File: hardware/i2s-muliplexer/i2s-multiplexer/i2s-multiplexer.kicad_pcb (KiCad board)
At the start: 2 copper layers, 80 x 50 mm, 35 parts, among them J1 Conn_01x05, J2 Conn_01x05, J3 Conn_01x05, J4 Conn_01x05, J5 Conn_01x05, J6 Conn_01x05, J7 Conn_01x07, J8 Conn_01x05, U1 74HC244, U2 74HC244, U3 74HC244, U4 74HC126, U5 74LS138

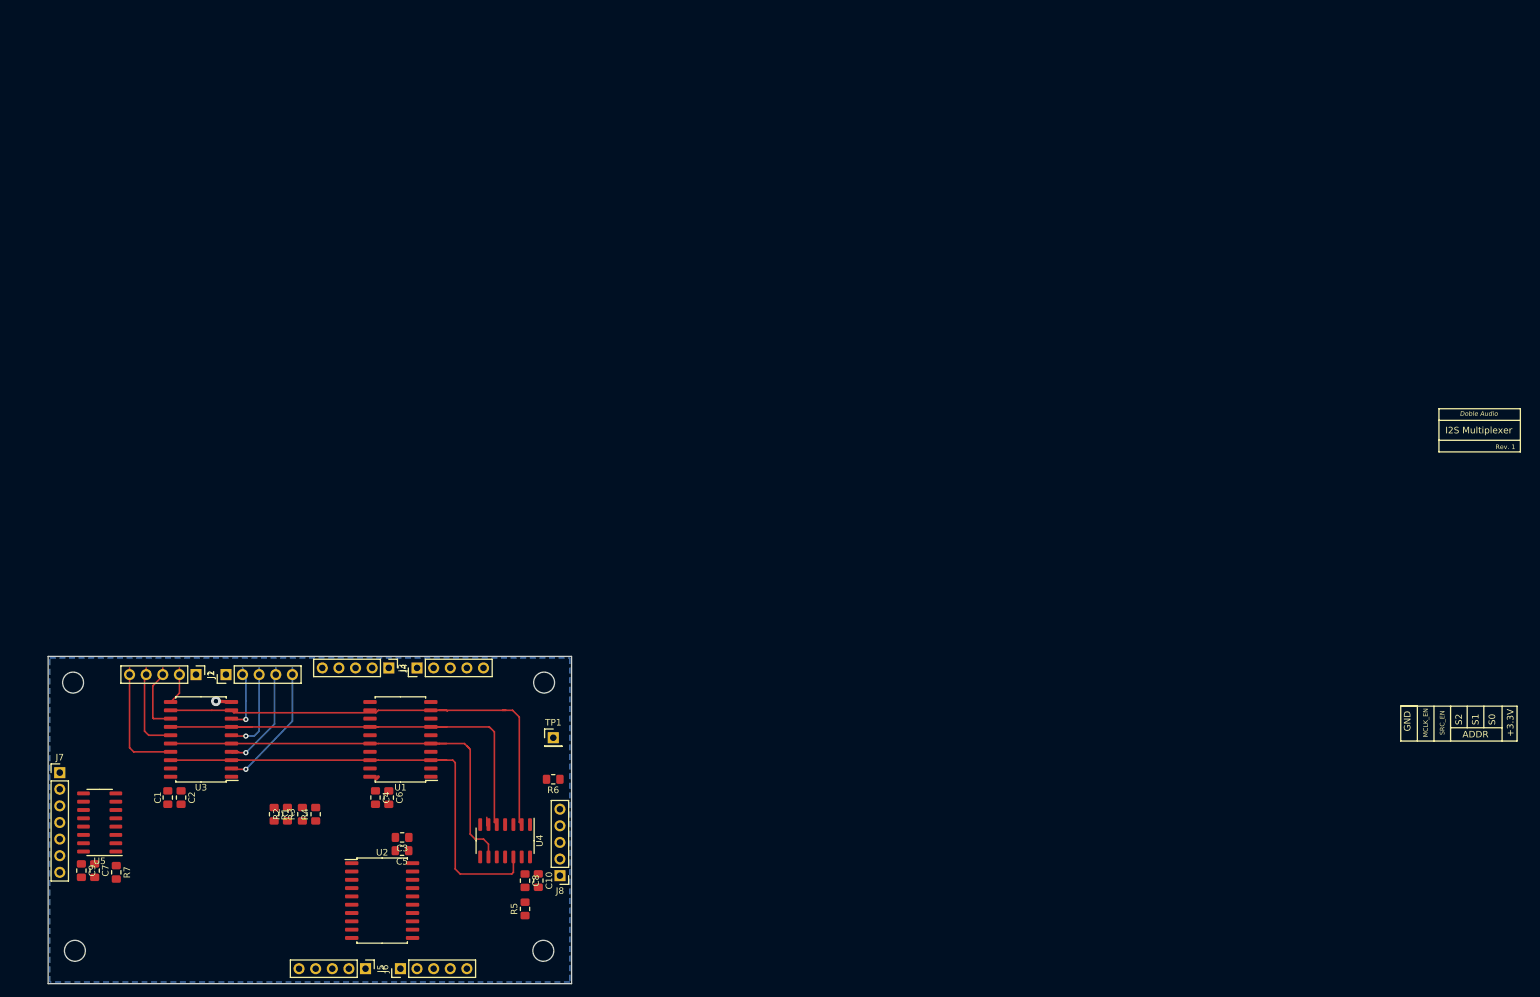
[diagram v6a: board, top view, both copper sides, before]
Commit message: Input trace track length tuning
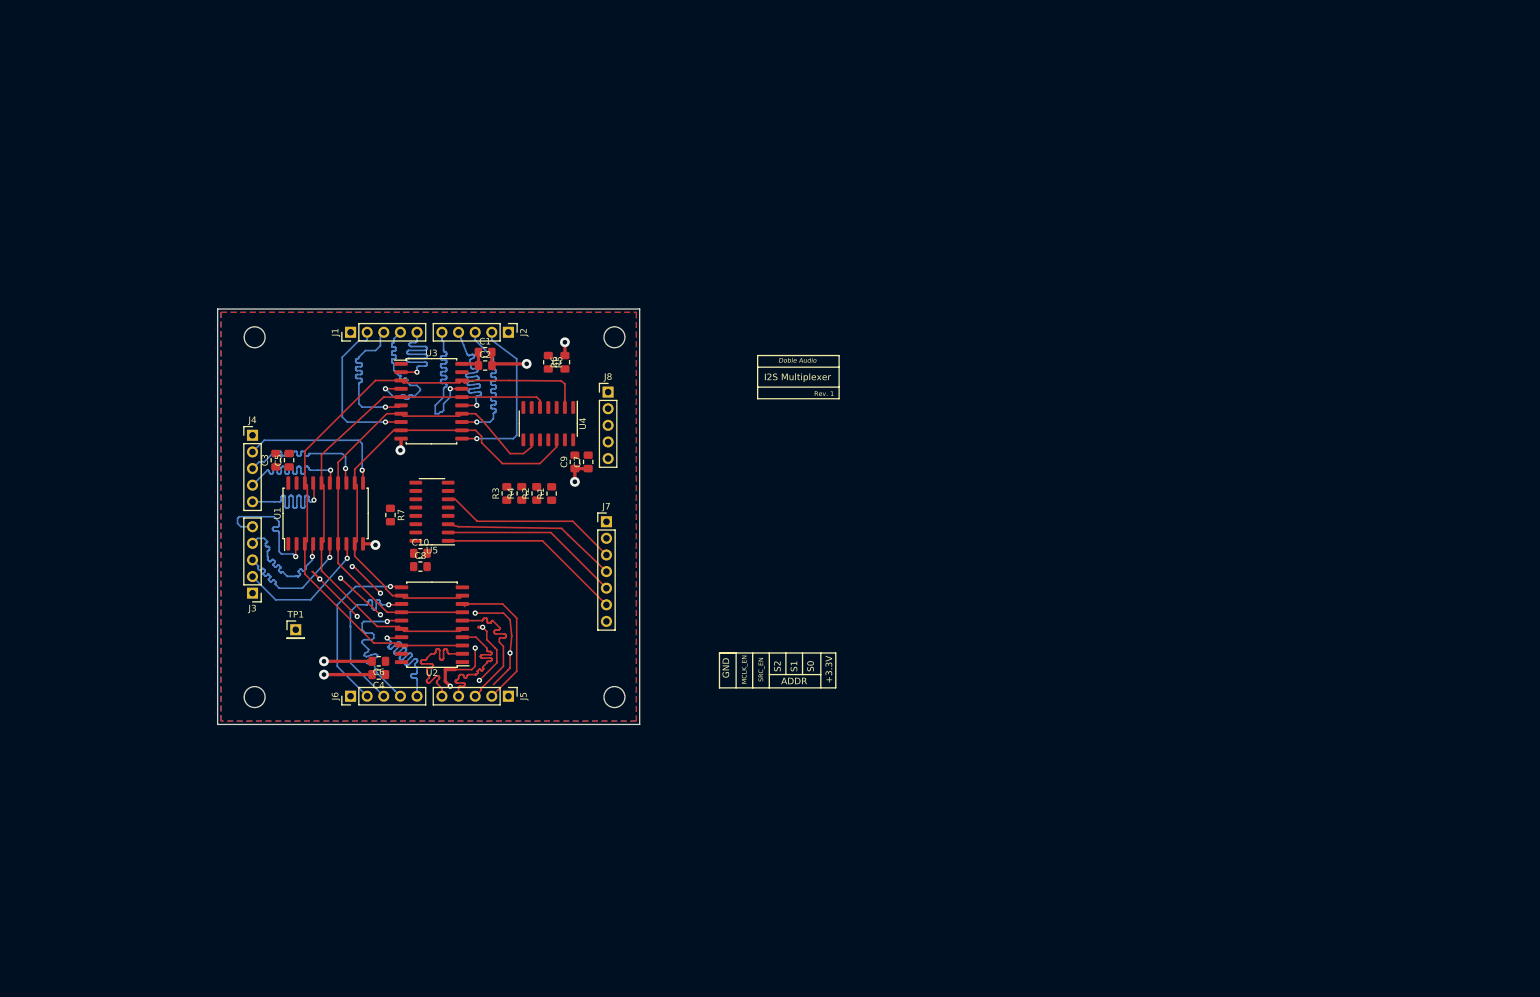
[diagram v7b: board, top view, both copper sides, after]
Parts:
- removed the REF** at (30.0, 171.0)
- removed the REF** at (101.6, 171.0)
- removed the REF** at (29.7, 130.0)
- removed the REF** at (101.7, 130.0)
- added REF**: MountingHole_3.2mm_M3_ISO7380, MountingHole:MountingHole_3.2mm_M3_ISO7380, F.Cu at (57.5, 132.2)
- added REF**: MountingHole_3.2mm_M3_ISO7380, MountingHole:MountingHole_3.2mm_M3_ISO7380, F.Cu at (112.5, 132.2)
- added REF**: MountingHole_3.2mm_M3_ISO7380, MountingHole:MountingHole_3.2mm_M3_ISO7380, F.Cu at (57.5, 77.2)
- added REF**: MountingHole_3.2mm_M3_ISO7380, MountingHole:MountingHole_3.2mm_M3_ISO7380, F.Cu at (112.5, 77.2)
- moved C9 97.9 mm to (106.4, 96.3), turned to 90 degrees
- moved C7 97.9 mm to (108.5, 96.3), turned to 90 degrees
- moved J7 91.9 mm to (111.3, 105.4)
- moved R5 83.6 mm to (102.4, 81.0), turned to 270 degrees
- moved C1 83.6 mm to (92.7, 79.5), turned to 0 degrees
- moved C2 80.8 mm to (92.7, 81.5), turned to 0 degrees
- moved J8 74.3 mm to (111.5, 85.6), turned to 0 degrees
- moved J2 70.8 mm to (96.3, 76.5)
- moved U5 69.5 mm to (84.6, 103.9)
- moved R7 68.8 mm to (78.2, 104.4)
- moved R1 64.8 mm to (102.9, 101.1), turned to 90 degrees
- moved U4 64.1 mm to (102.4, 90.4)
- moved R6 63.8 mm to (104.9, 81.0), turned to 90 degrees
- moved U3 62.6 mm to (84.5, 87.0), turned to 0 degrees
- moved C5 62.1 mm to (62.7, 96.0), turned to 90 degrees
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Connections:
- C3 pad 1: +3V3 -> GND
- C3 pad 2: GND -> +3V3
- C5 pad 1: +3V3 -> GND
- C5 pad 2: GND -> +3V3
- C7 pad 1: +3V3 -> GND
- C7 pad 2: GND -> +3V3
- C9 pad 1: +3V3 -> GND
- C9 pad 2: GND -> +3V3
- U4 pad 1: MCLK_EN -> Net-(R5-Pad2)
- U4 pad 11: LRCLK_OUT -> MCLK_OUT
- U4 pad 12: /LRCLK -> /MCLK
- U4 pad 13: Net-(R5-Pad2) -> MCLK_EN
- U4 pad 2: /MCLK -> /LRCLK
- U4 pad 3: MCLK_OUT -> LRCLK_OUT
- U4 pad 5: /DATA -> /BCLK
- U4 pad 6: DATA_OUT -> BCLK_OUT
- U4 pad 8: BCLK_OUT -> DATA_OUT
- U4 pad 9: /BCLK -> /DATA
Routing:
- net GND: track 2.37 -> 95.7 mm, vias 1 -> 19
- net A0: track 0.00 -> 28.2 mm
- net SRC_EN: track 0.00 -> 27.7 mm
- net A1: track 0.00 -> 27.7 mm
- net A2: track 0.00 -> 26.9 mm
- net MCLK_0: track 0.00 -> 26.9 mm, vias 0 -> 1
- net LRCLK_0: track 0.00 -> 26.9 mm, vias 0 -> 1
- net DATA_0: track 0.00 -> 26.9 mm, vias 0 -> 1
- net BCLK_0: track 0.00 -> 26.9 mm, vias 0 -> 1
- net /LRCLK: track 72.7 -> 97.0 mm
- net DATA_2: track 0.00 -> 23.9 mm, vias 0 -> 1
- net BCLK_2: track 0.00 -> 23.9 mm, vias 0 -> 1
- net LRCLK_2: track 0.00 -> 23.8 mm, vias 0 -> 1
- net MCLK_2: track 0.00 -> 23.8 mm, vias 0 -> 1
- net MCLK_1: track 0.00 -> 23.3 mm
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- added copper zone on F.Cu, net +3V3
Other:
- board size 80 x 50 mm -> 64.5 x 63.5 mm

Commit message: Updated to KiCad 6
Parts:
- C1, C10, C2, C3, C4, C5, C6, C7, C8, C9: footprint Capacitor_SMD:C_0805_2012Metric_Pad1.15x1.40mm_HandSolder -> Capacitor_SMD:C_0805_2012Metric_Pad1.18x1.45mm_HandSolder
- R1, R2, R3, R4, R5, R6, R7: footprint Resistor_SMD:R_0805_2012Metric_Pad1.15x1.40mm_HandSolder -> Resistor_SMD:R_0805_2012Metric_Pad1.20x1.40mm_HandSolder
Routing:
- net /MCLK: track 71.1 -> 74.4 mm
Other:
- net class Default removed
- net class Power removed
